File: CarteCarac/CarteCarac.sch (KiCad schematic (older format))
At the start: 8 parts, among them J1 Conn_02x25_Top_Bottom_Mountin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

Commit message: v0 near finished
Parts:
- removed RthB0: PT1000, Resistor_SMD:R_0603_1608Metric_Pad1.05x0.95mm_HandSolder, symbol Sensor_Temperature:PT1000
- added H10, H9: MountingHole_Pad, MountingHole:MountingHole_3.2mm_M3_Pad_Via, symbol Mechanical:MountingHole_Pad
- added J2: Conn_02x39_Top_Bottom_MountingPin, LibPersoNadj:db_78f_09565527613, symbol Connector_Generic_MountingPin:Conn_02x39_Top_Bottom_MountingPin
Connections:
- net labels added: +RX10, +RX12, +RX32, +RX34, +RY10, +RY12, +RY32, +RY34, +RZ10, +RZ12, +RZ32, +RZ34, -RX10, -RX12, -RX32, -RX34, -RY10, -RY12, -RY32, -RY34, -RZ10, -RZ12, -RZ32, -RZ34
- wire segments 117 -> 221
- no-connect marks 7 -> 1
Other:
- note added: "Connecteur 78:\n\nFrom 15P(1-15):\nB*\nCR*\nPT1000 A\nM*\nSh*\n\n\nFrom 25S(26-50):\n\nRTN* (both)\nS*\nPT1000 A & B\nPWR_Shield*\n+6V*\nCAL\nCAL_RTN\nShield*\nCAL_Shield\n\n\nAdded:\n\nIn2P*\nV_Bias*\nVDD*\nR34* + & -\nR32* + & - ( - = +R34 )\nR12* + & - ( - = VDD )\nR10* + & - ( - = V_Bias )\n\n* for X Y and Z"
- moved on the sheet: H5, H6, H7, H8, J1, TP_Pot1, TP_Pot2

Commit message: Routé, verif pre-envoie
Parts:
- J_50m_1: renamed from J1; footprint LibPersoNadj:DD50S564TLF -> LibPersoNadj:db_50m_MP_DD50S564TXLF
- J_78f_1: renamed from J2; footprint LibPersoNadj:db_78f_09565527613 -> LibPersoNadj:db_78f_MP_09565527613
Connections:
- net RTNx renamed Sx-
- net RTNy renamed Sy-
- net RTNz renamed Sz-
- net Sx renamed Sx+
- net Sy renamed Sy+
- net Sz renamed Sz+
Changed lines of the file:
@@
 RTN_B
 Wire Wire Line
-	1625 9325 1350 9325
+	1725 9025 1450 9025
 Text Label 1050 7125 0    50   ~ 0
 CR_Z
@@
 B_Z
 $Comp
-L Connector_Generic_MountingPin:Conn_02x25_Top_Bottom_MountingPin J1
+L Connector_Generic_MountingPin:Conn_02x25_Top_Bottom_MountingPin J_50m_1
 U 1 1 5E725E95
 P 1925 7825
-F 0 "J1" H 1975 9242 50  0000 C CNN
+F 0 "J_50m_1" H 1975 9242 50  0000 C CNN
 F 1 "Conn_02x25_Top_Bottom_MountingPin" H 1975 9151 50  0000 C CNN
-F 2 "LibPersoNadj:DD50S564TLF" H 1925 7825 50  0001 C CNN
+F 2 "LibPersoNadj:db_50m_MP_DD50S564TXLF" H 1925 7825 50  0001 C CNN
 F 3 "~" H 1925 7825 50  0001 C CNN
 	1    1925 7825
@@
 Wire Wire Line
 	5550 7475 5725 7475
-NoConn ~ 1350 9325
+NoConn ~ 1450 9025
 Wire Wire Line
 	9800 1325 9125 1325
@@
 $EndComp
 $Comp
-L power:PWR_FLAG #FLG0101
-U 1 1 5E1908E5
-P 2125 4975
-F 0 "#FLG0101" H 2125 5050 50  0001 C CNN
-F 1 "PWR_FLAG" V 2125 5102 50  0000 L CNN
-F 2 "" H 2125 4975 50  0001 C CNN
-F 3 "~" H 2125 4975 50  0001 C CNN
-	1    2125 4975
-	0    -1   1    0
-$EndComp
-Wire Wire Line
-	2125 4975 2175 4975
-$Comp
-L Connector_Generic_MountingPin:Conn_02x39_Top_Bottom_MountingPin J2
+L Connector_Generic_MountingPin:Conn_02x39_Top_Bottom_MountingPin J_78f_1
 U 1 1 5E1908EC
 P 2125 2700
-F 0 "J2" H 2175 4817 50  0000 C CNN
+F 0 "J_78f_1" H 2175 4817 50  0000 C CNN
 F 1 "Conn_02x39_Top_Bottom_MountingPin" H 2175 4726 50  0000 C CNN
-F 2 "LibPersoNadj:db_78f_09565527613" H 2125 2700 50  0001 C CNN
+F 2 "LibPersoNadj:db_78f_MP_09565527613" H 2125 2700 50  0001 C CNN
 F 3 "~" H 2125 2700 50  0001 C CNN
 	1    2125 2700
@@
 Text Label 925  2900 0    50   ~ 0
 VDD_X
-Wire Wire Line
-	2175 4975 2175 5025
-Connection ~ 2175 4975
 Wire Wire Line
 	3325 3100 3325 4875
@@
 	2425 3100 3325 3100
 Connection ~ 2175 4875
-Wire Wire Line
-	2175 4875 2175 4975
 Wire Wire Line
 	9100 2325 9800 2325
@@
 	6075 7475 6425 7475
 Connection ~ 6075 7475
+Wire Wire Line
+	2175 4875 2175 5025
+Text GLabel 3100 800  2    50   Input ~ 0
+Sy+
+Text GLabel 3100 900  2    50   Input ~ 0
+Sy-
+Text GLabel 925  3600 0    50   Input ~ 0
+Sz+
+Text GLabel 925  3700 0    50   Input ~ 0
+Sz-
+Text GLabel 925  3300 0    50   Input ~ 0
+Sx-
+Text GLabel 925  3400 0    50   Input ~ 0
+Sx+
 $EndSCHEMATC

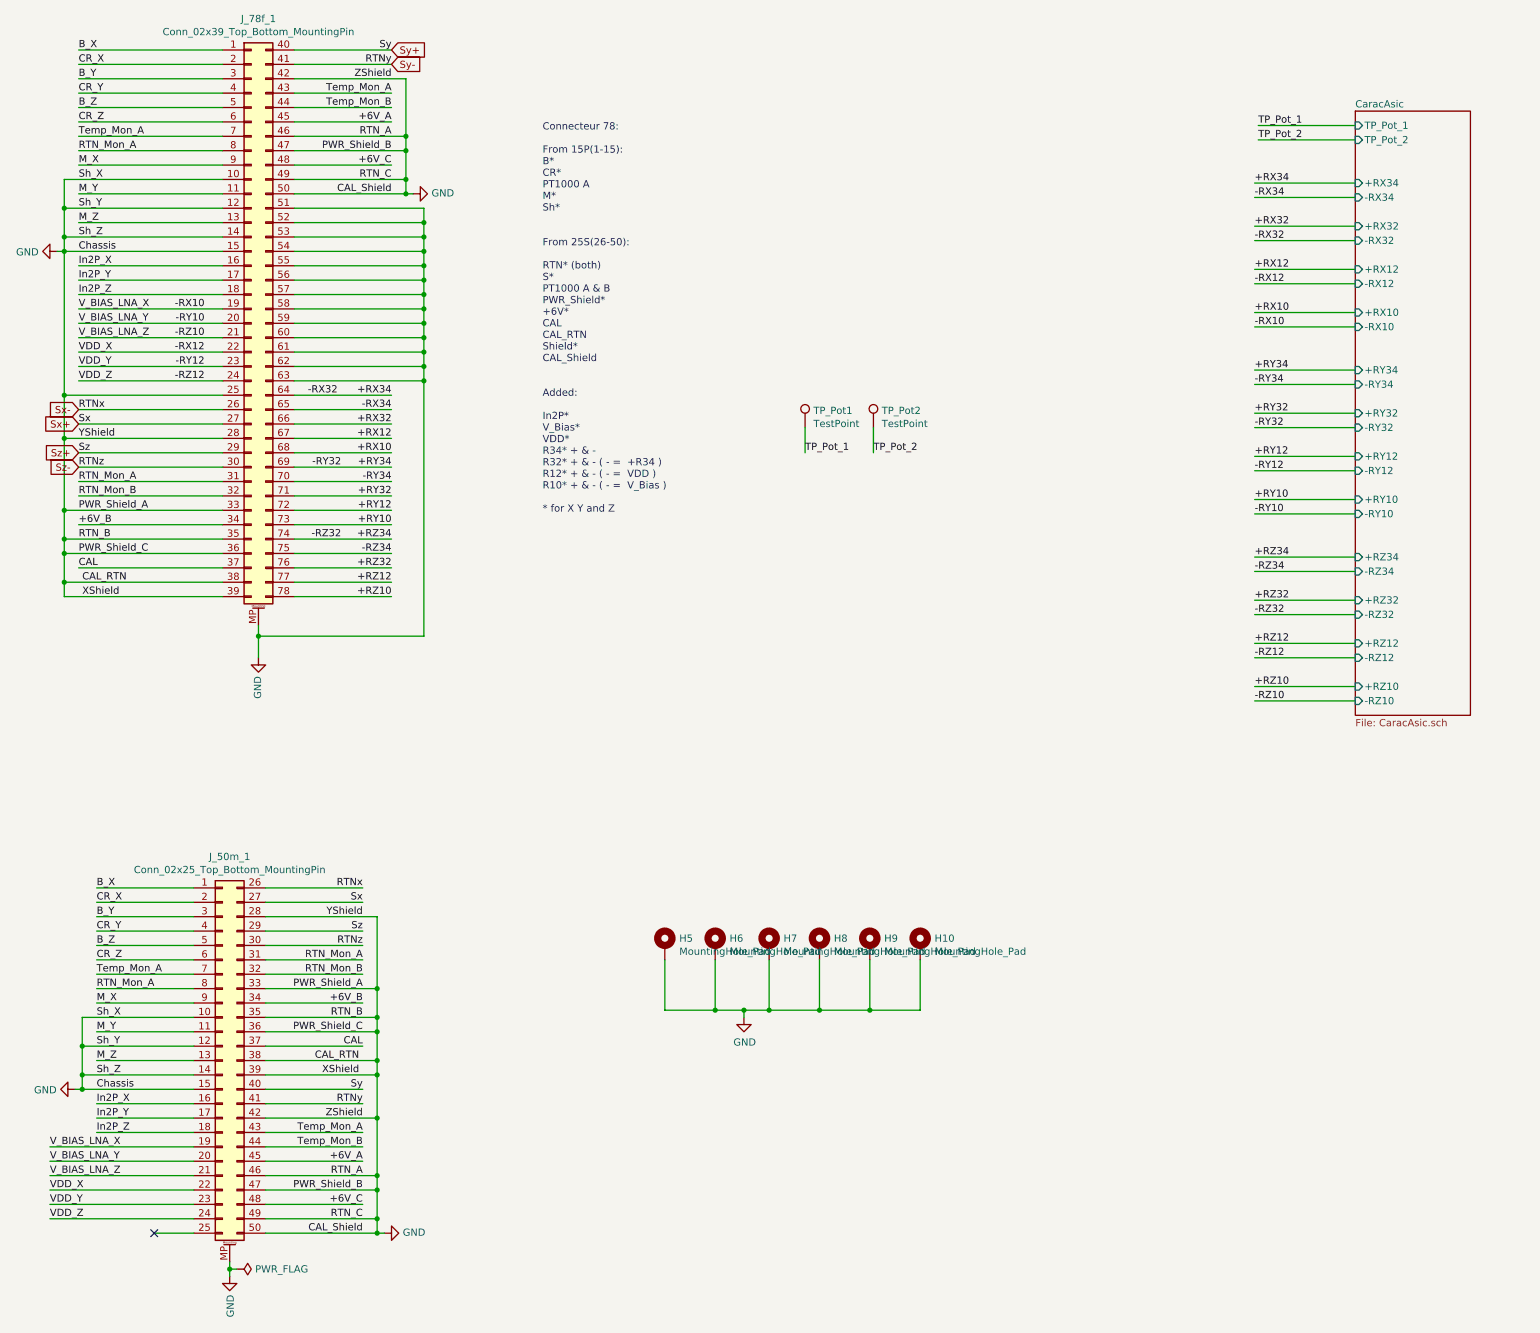
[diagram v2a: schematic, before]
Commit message: Correction pinout 6P3T & ajout d'étiquettes sur pin hiérarchique 3P4T + routage
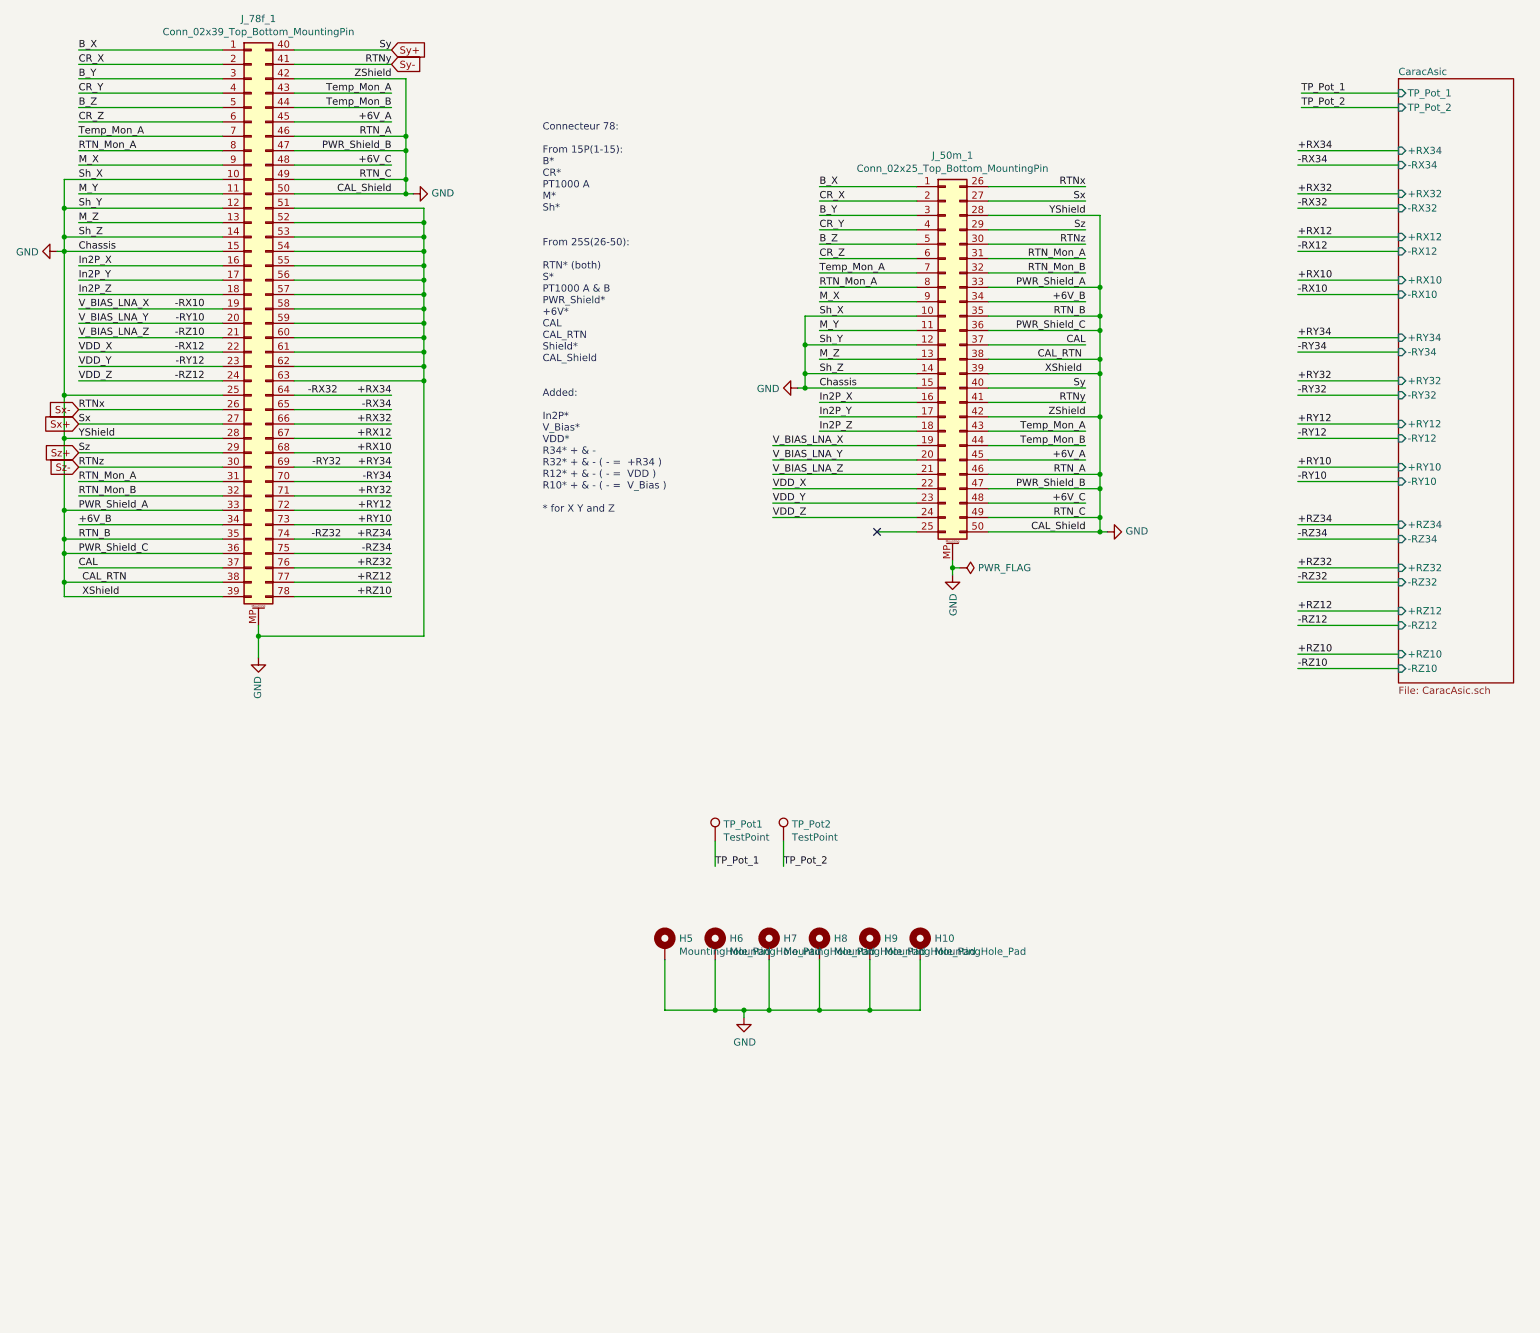
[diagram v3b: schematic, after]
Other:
- moved on the sheet: J_50m_1, TP_Pot1, TP_Pot2
